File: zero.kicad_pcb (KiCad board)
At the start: 2 copper layers, 266 x 76 mm, 74 parts, among them SW101 SW_Push, SW102 SW_Push, SW103 SW_Push, SW104 SW_Push, SW105 SW_Push, SW106 SW_Push, SW107 SW_Push, SW108 SW_Push, SW109 SW_Push, SW110 SW_Push, SW111 SW_Push, SW112 SW_Push, SW201 SW_Push, SW202 SW_Push, SW203 SW_Push, SW204 SW_Push, SW205 SW_Push, SW206 SW_Push, SW207 SW_Push, SW208 SW_Push, SW209 SW_Push, SW210 SW_Push, SW211 SW_Push, SW212 SW_Push, SW404 SW_Push, SW405 SW_Push, SW406 SW_Push, SW407 SW_Push, SW408 SW_Push, SW409 SW_Push, U1 Pico

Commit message: REV 1
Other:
- board text added: "CHORD ZERO REV 1"
- board text removed: "CHORD ZERO, REV 0"
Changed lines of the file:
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@@
     (effects (font (size 1 1) (thickness 0.15)))
   )
-  (gr_text "CHORD ZERO, REV 0" (at -57 75) (layer "F.SilkS")
+  (gr_text "CHORD ZERO REV 1" (at -57 75) (layer "F.SilkS")
     (effects (font (size 1 1) (thickness 0.15)))
   )

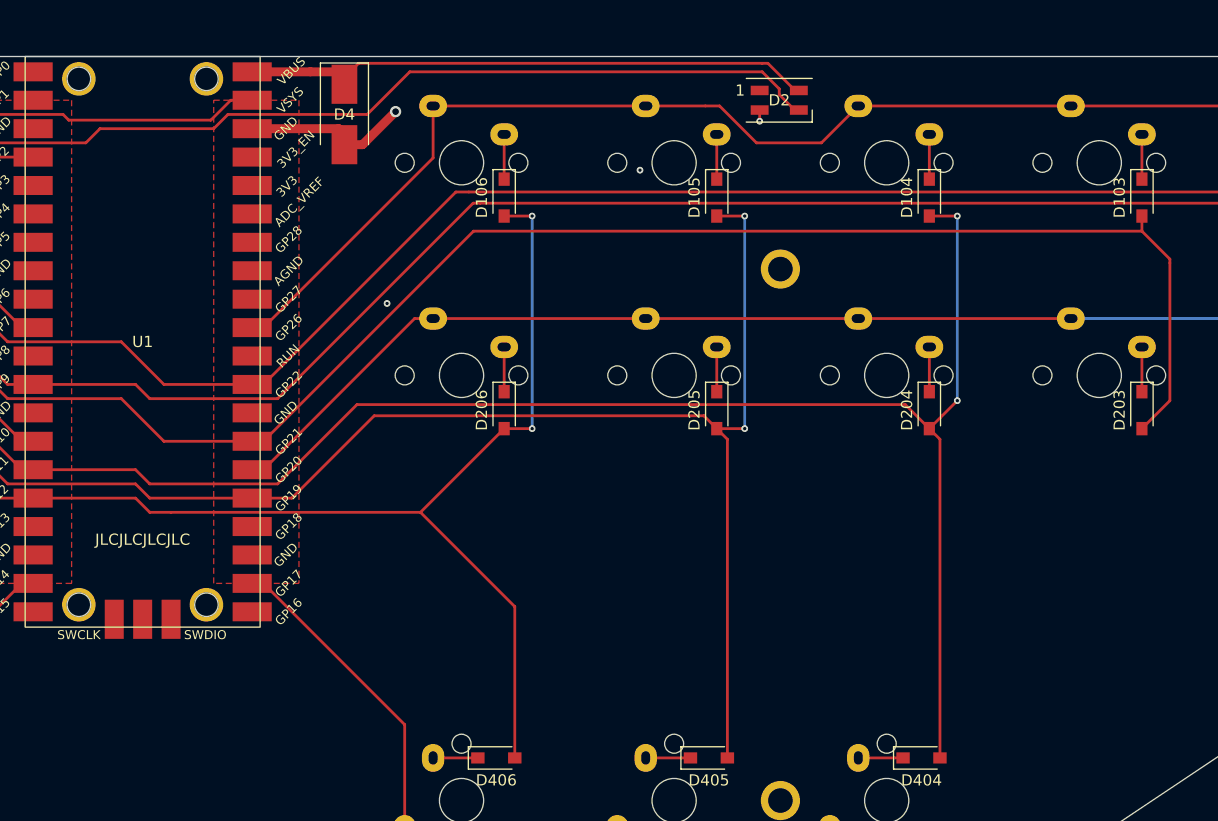
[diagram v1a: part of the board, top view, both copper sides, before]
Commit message: Add logo on backside
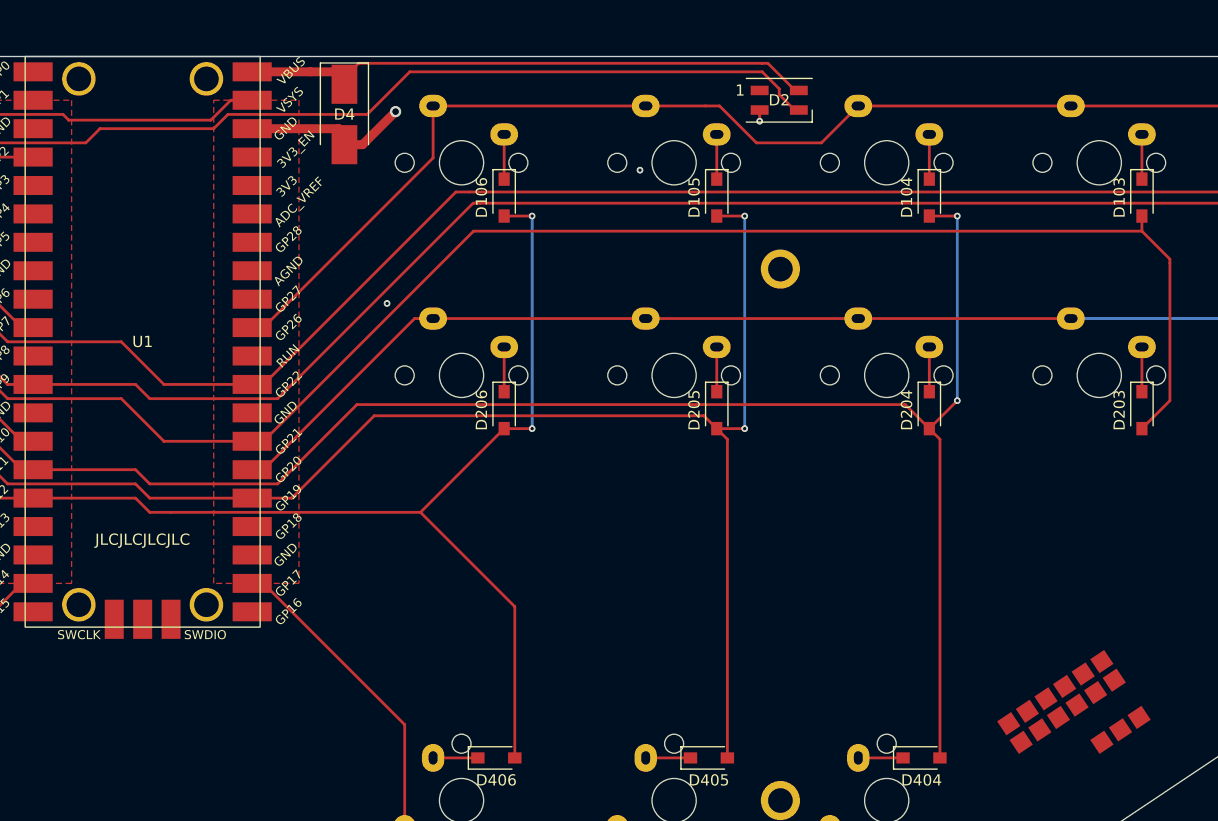
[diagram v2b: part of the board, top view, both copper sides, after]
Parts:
- added LOGO_1: CHORD LOGO, footprints:chord_logo_3d, F.Cu at (85.7, 57.1)
